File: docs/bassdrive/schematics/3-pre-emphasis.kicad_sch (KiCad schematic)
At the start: 7 parts

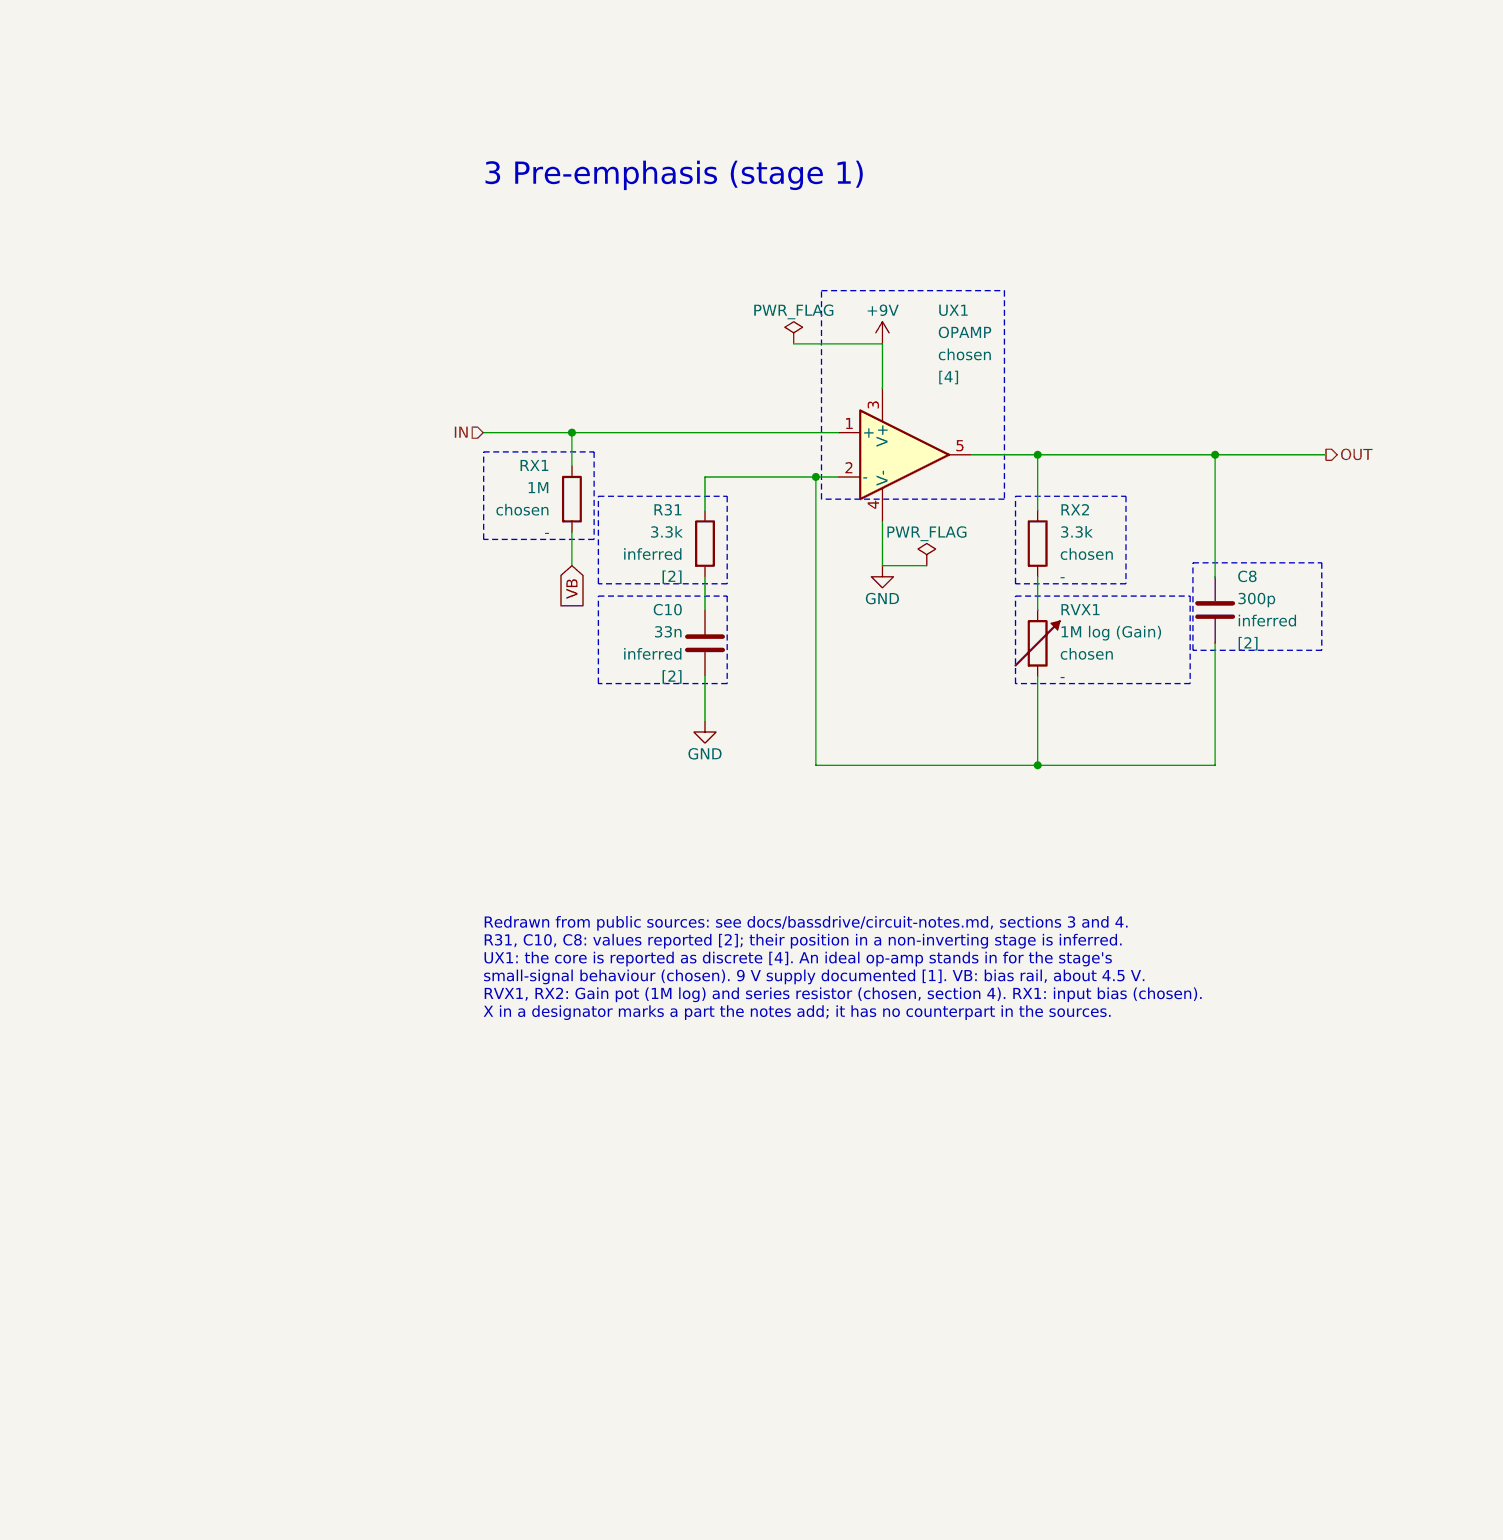
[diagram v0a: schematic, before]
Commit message: Generate KiCad schematics for every effect and make them standard (#85)
* chore: save work

* Generate KiCad schematics for every effect and make them standard (closes #11)

Every effect with circuit notes now has a KiCad schematic of its modelled
circuit, generated from tools/schematics/<name>.py by the new kicadsch and
stages modules: BassDrive (#11), BassPreamp and MidHump. Each script checks
its corner frequencies and gains against the notes and DSP constants.

make schematic-sources regenerates the sheets, make schematic-check (a new
docs-workflow step) fails if they are stale, and the schematics-present
pre-commit hook fails if an effect with circuit notes has none. AGENTS.md,
the effect skill and the developer guides now treat the schematic as a
required step. The sheets are embedded next to their sections in each
effect's circuit notes, and the disagreements drawing them revealed are
recorded as open questions.

Co-Authored-By: Claude Opus 5.5 <noreply@anthropic.com>

---------

Co-authored-by: Claude Opus 5.5 <noreply@anthropic.com>
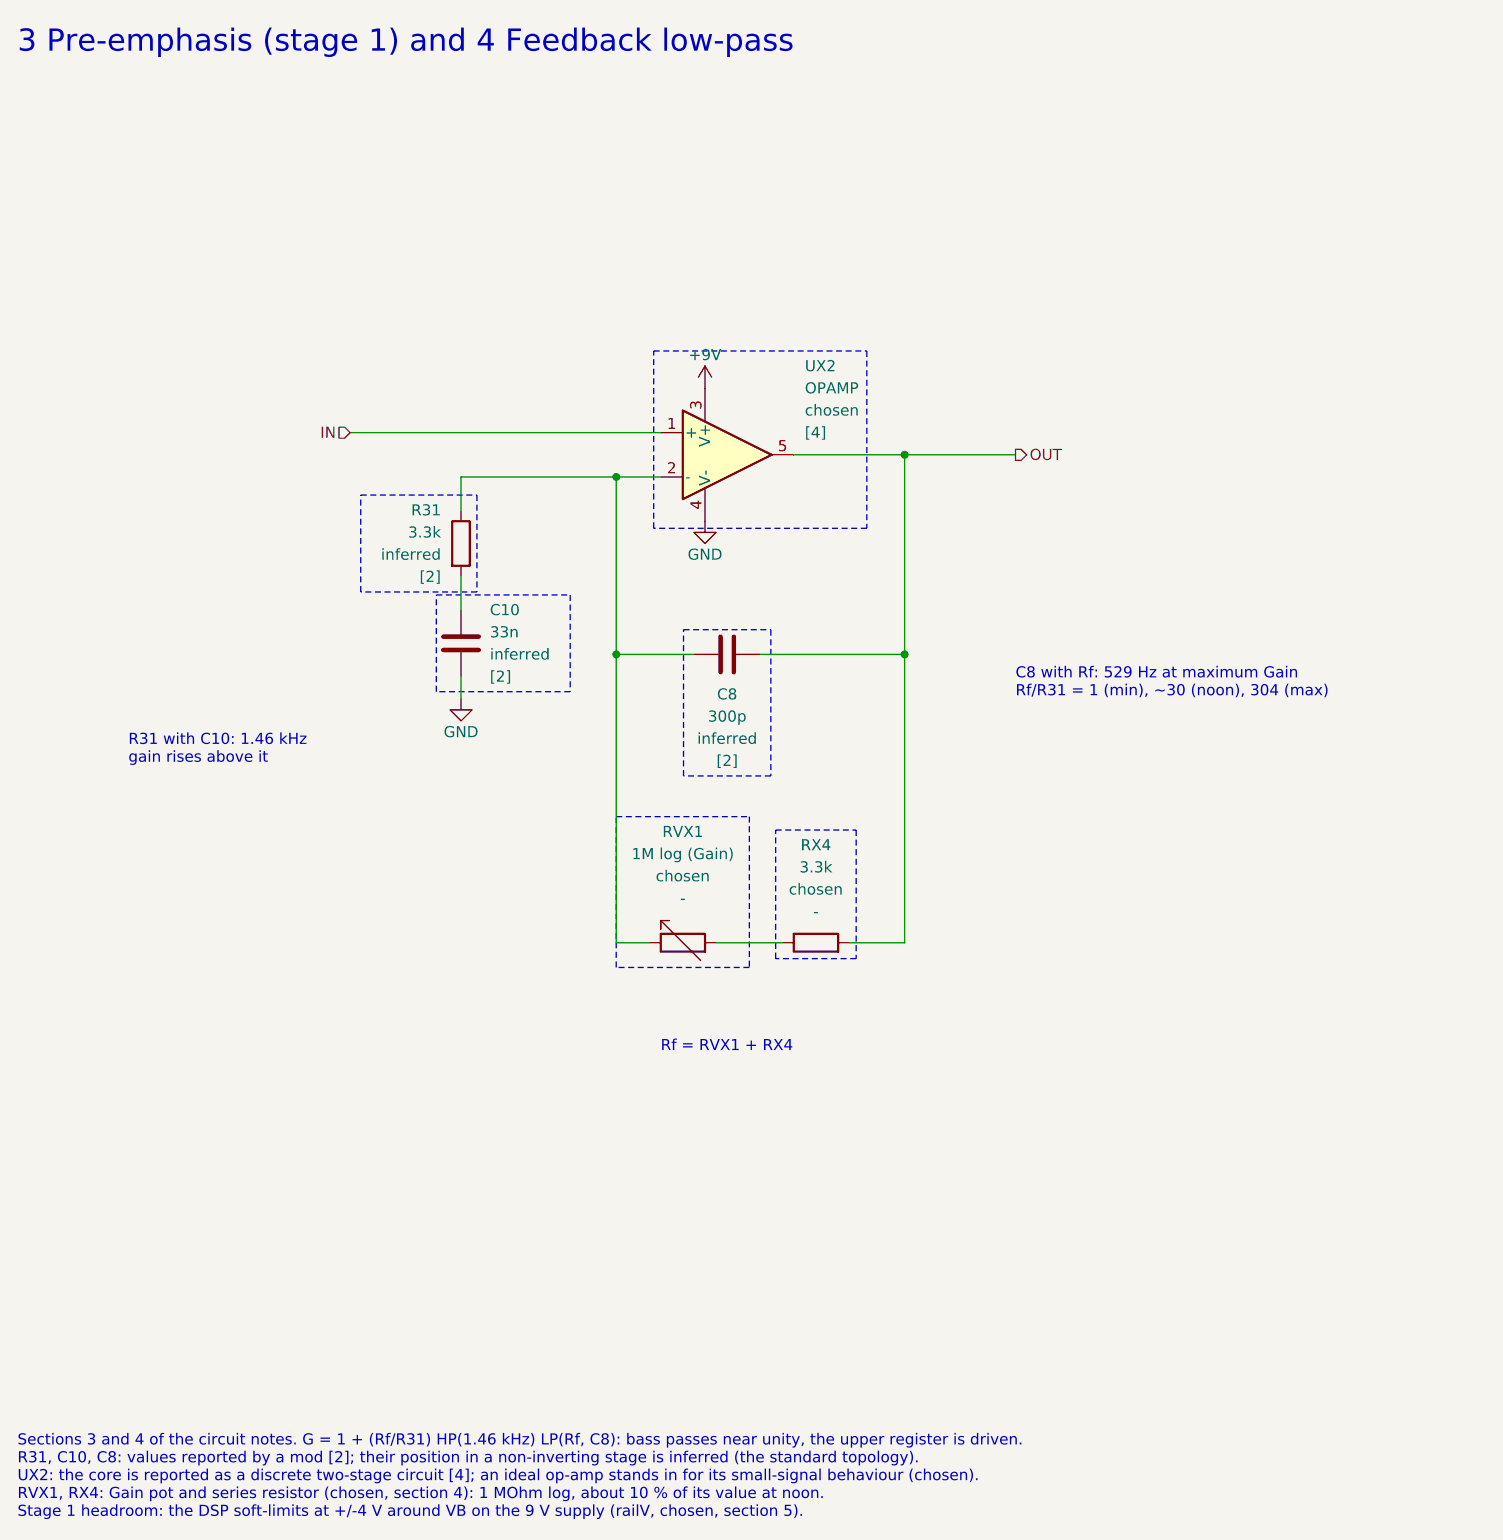
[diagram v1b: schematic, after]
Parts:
- removed RX1: 1M, symbol Device:R
- removed RX2: 3.3k, symbol Device:R
- removed UX1: OPAMP, symbol Simulation_SPICE:OPAMP
- added RX4: 3.3k, symbol Device:R
- added UX2: OPAMP, symbol Simulation_SPICE:OPAMP
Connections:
- net +9V: now also UX2.3 (V+)
- net GND: now also UX2.4 (V-)
- net IN: now also UX2.1 (+)
- net OUT: now also C8.2, RX4.2, UX2.5; no longer C8.1
- net at RVX1.1: now also C8.1, R31.1, UX2.2 (-)
- new net: RVX1.2, RX4.1
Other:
- note added: "3 Pre-emphasis (stage 1) and 4 Feedback low-pass"
- note added: "C8 with Rf: 529 Hz at maximum Gain Rf/R31 = 1 (min), ~30 (noon), 304 (max)"
- note added: "R31 with C10: 1.46 kHz gain rises above it"
- note added: "Rf = RVX1 + RX4"
- note added: "Sections 3 and 4 of the circuit notes. G = 1 + (Rf/R31) HP(1.46 kHz) LP(Rf, C8): bass passes near unity, the upper register is driven. R31, C10, C8: values reported by a mod [2]; their position in a non-inverting stage is inferred (the standard topology). UX2: the core is reported as a discrete two-stage circuit [4]; an ideal op-amp stands in for its small-signal behaviour (chosen). RVX1, RX4: Ga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"
- note removed: "3 Pre-emphasis (stage 1)"
- note removed: "Redrawn from public sources: see docs/bassdrive/circuit-notes.md, sections 3 and 4. R31, C10, C8: values reported [2]; their position in a non-inverting stage is inferred. UX1: the core is reported as discrete [4]. An ideal op-amp stands in for the stage's small-signal behaviour (chosen). 9 V supply documented [1]. VB: bias rail, about 4.5 V. RVX1, RX2: Gain pot (1M log) and series resistor (chos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"
